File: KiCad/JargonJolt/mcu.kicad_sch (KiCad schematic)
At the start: 19 parts, among them J1 Conn_01x05, Q1 SS8050-G, Q2 SS8050-G, SW1 SW_Push, SW2 SW_Push, U1 ESP32-S3-WROOM-1-N16R2

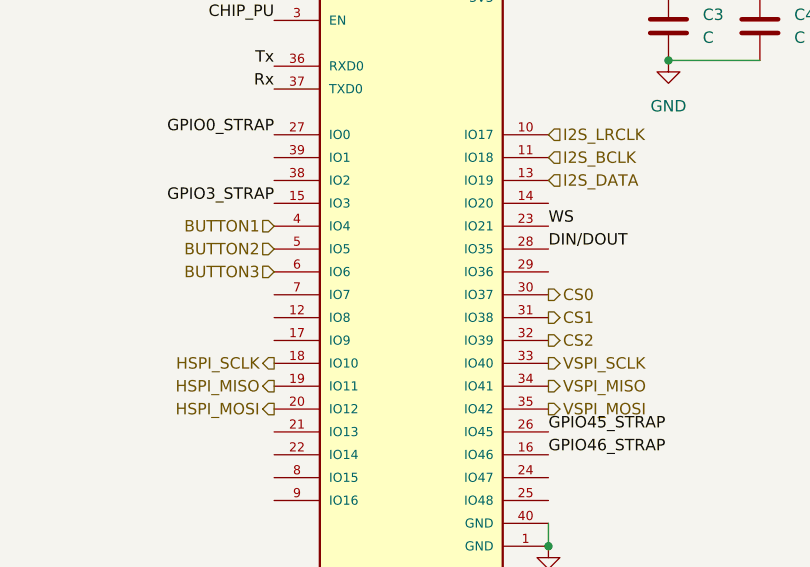
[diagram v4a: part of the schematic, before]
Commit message: added more footprints
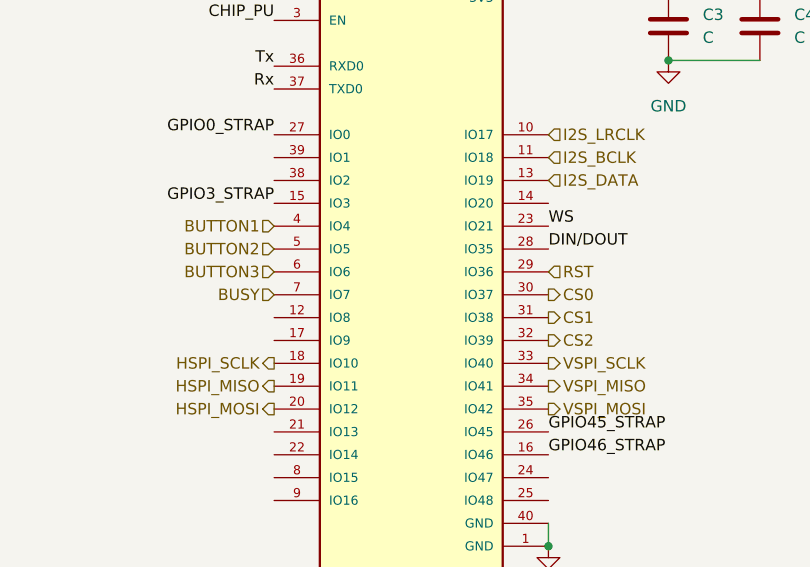
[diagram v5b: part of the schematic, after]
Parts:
- J1: footprint (none) -> Connector_PinSocket_2.54mm:PinSocket_1x05_P2.54mm_Vertical
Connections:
- net RST: now reaches U1.29 (IO36)
- net BUSY: now reaches U1.7 (IO7)
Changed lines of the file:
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@@
+    (effects (font (size 1.27 1.27)) (justify left))
+  )
+  (hierarchical_label "RST" (shape input) (at 202.565 85.725 0) (fields_autoplaced)
     (effects (font (size 1.27 1.27)) (justify left))
   )
@@
   )
   (hierarchical_label "HSPI_MISO" (shape output) (at 172.085 98.425 180) (fields_autoplaced)
+    (effects (font (size 1.27 1.27)) (justify right))
+  )
+  (hierarchical_label "BUSY" (shape input) (at 172.085 88.265 180) (fields_autoplaced)
     (effects (font (size 1.27 1.27)) (justify right))
   )
@@
       (effects (font (size 1.27 1.27)) (justify left))
     )
-    (property "Footprint" "" (at 31.115 115.57 0)
-      (effects (font (size 1.27 1.27)) hide)
-    )
+    (property "Footprint" "Connector_PinSocket_2.54mm:PinSocket_1x05_P2.54mm_Vertical" (at 31.115 115.57 0)
+      (effects (font (size 1.27 1.27)) hide)
+    )

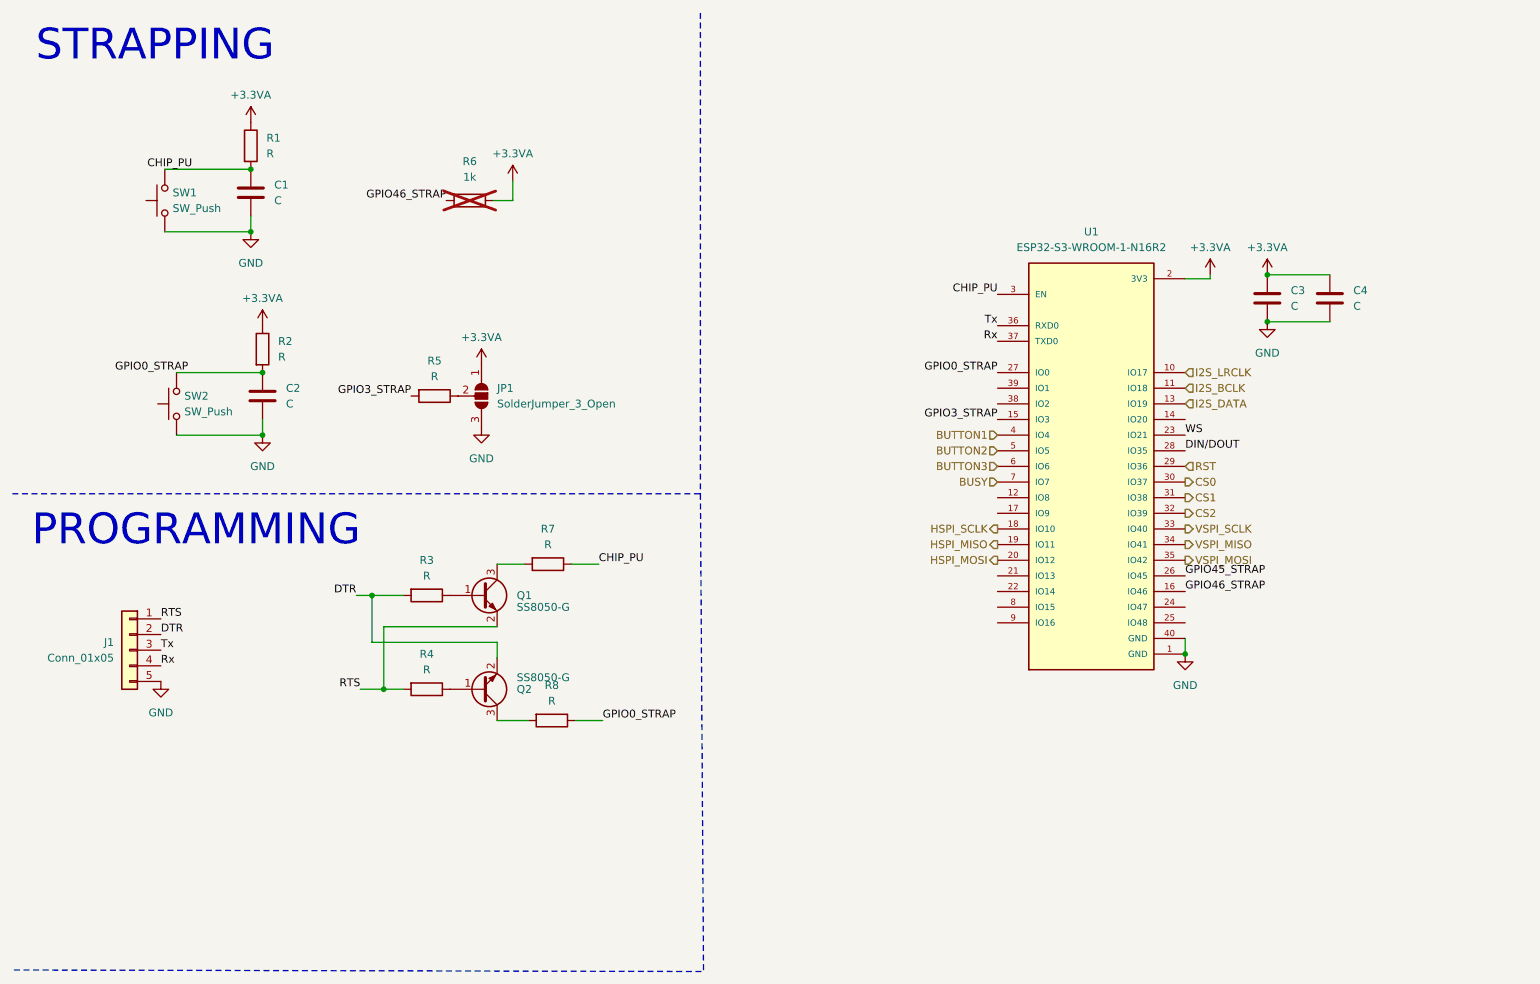
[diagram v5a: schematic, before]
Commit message: PCB first revision
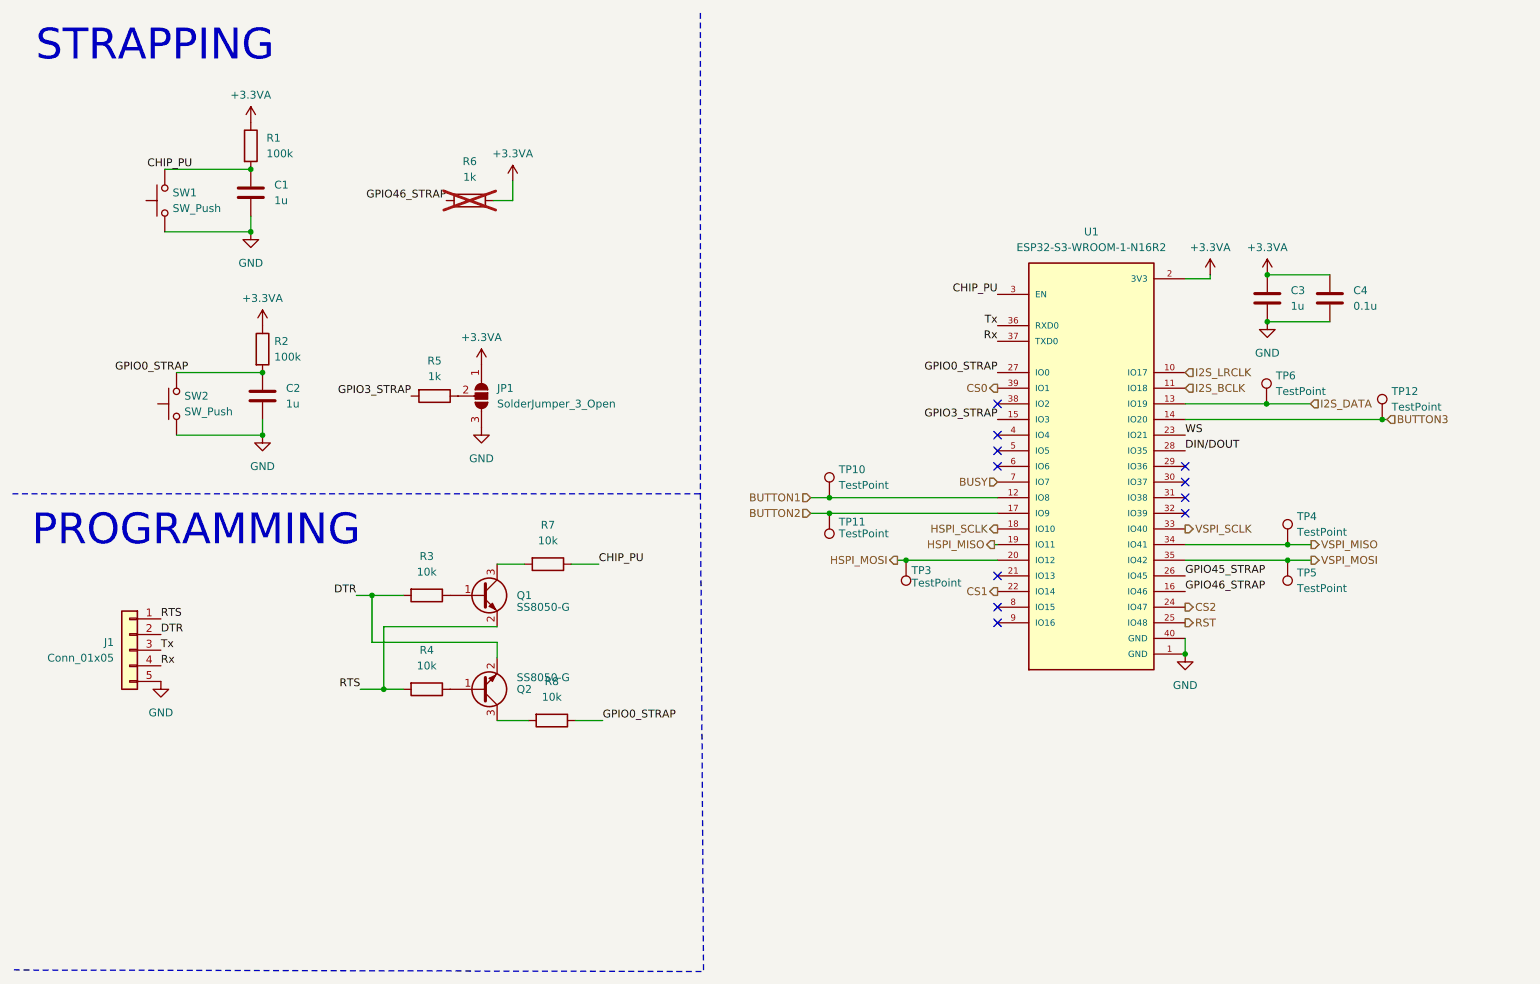
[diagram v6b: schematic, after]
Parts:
- added TP10, TP11, TP12, TP3, TP4, TP5, TP6: TestPoint, TestPoint:TestPoint_Pad_D1.5mm, symbol Connector:TestPoint
- C1, C2, C3: value C -> 1u
- C4: value C -> 0.1u
- JP1: footprint (none) -> Jumper:SolderJumper-3_P1.3mm_Open_RoundedPad1.0x1.5mm
- R1, R2: value R -> 100k
- R3, R4, R7, R8: value R -> 10k
- R5: value R -> 1k
- SW1, SW2: footprint (none) -> Button_Switch_SMD:SW_Push_1P1T_NO_6x6mm_H9.5mm
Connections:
- net BUTTON1: now also U1.12 (IO8), TP10.1; no longer U1.4 (IO4)
- net BUTTON2: now also U1.17 (IO9), TP11.1; no longer U1.5 (IO5)
- net BUTTON3: now also U1.14 (IO20), TP12.1; no longer U1.6 (IO6)
- net CS0: now also U1.39 (IO1); no longer U1.30 (IO37)
- net CS1: now also U1.22 (IO14); no longer U1.31 (IO38)
- net CS2: now also U1.24 (IO47); no longer U1.32 (IO39)
- net HSPI_MOSI: now also TP3.1
- net I2S_DATA: now also TP6.1
- net RST: now also U1.25 (IO48); no longer U1.29 (IO36)
- net VSPI_MISO: now also TP4.1
- net VSPI_MOSI: now also TP5.1
- no-connect marks 0 -> 11

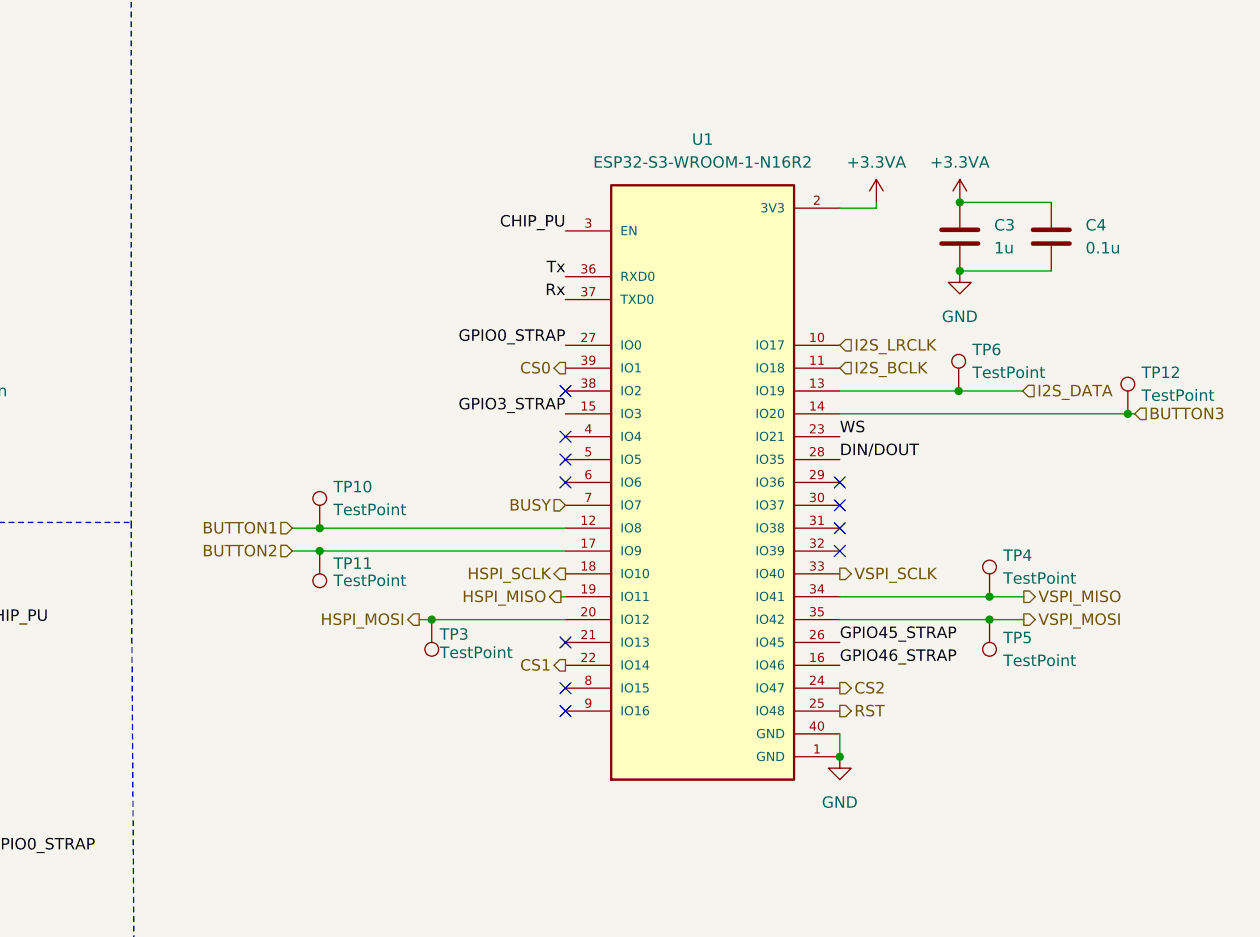
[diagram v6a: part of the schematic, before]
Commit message: added test leds
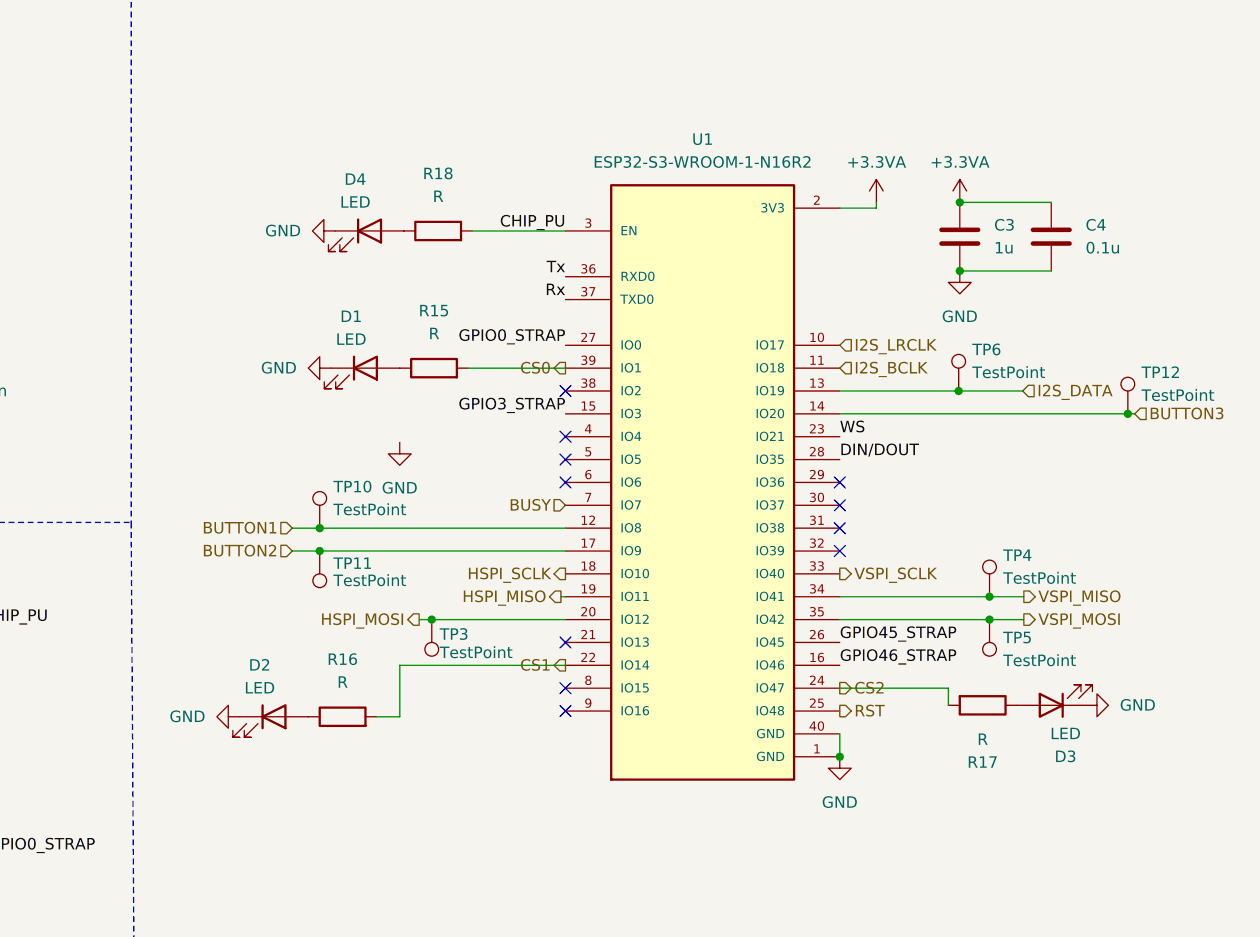
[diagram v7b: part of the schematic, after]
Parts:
- added D1, D2, D3, D4: LED, LED_SMD:LED_1206_3216Metric_Pad1.42x1.75mm_HandSolder, symbol Device:LED
- added R15, R16, R17, R18: R, Resistor_SMD:R_0805_2012Metric, symbol Device:R
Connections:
- net CHIP_PU: now also R18.2
- net CS0: now also R15.2
- net CS1: now also R16.2
- net CS2: now also R17.2
- net GND: now also D1.1 (K), D2.1 (K), D3.1 (K), D4.1 (K)
- new net: D4.2 (A), R18.1
- new net: D3.2 (A), R17.1
- new net: D1.2 (A), R15.1
- new net: D2.2 (A), R16.1
